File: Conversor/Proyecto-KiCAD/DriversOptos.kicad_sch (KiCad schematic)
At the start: 22 parts, among them U5 2ED21834-S06J, U6 2ED21834-S06J

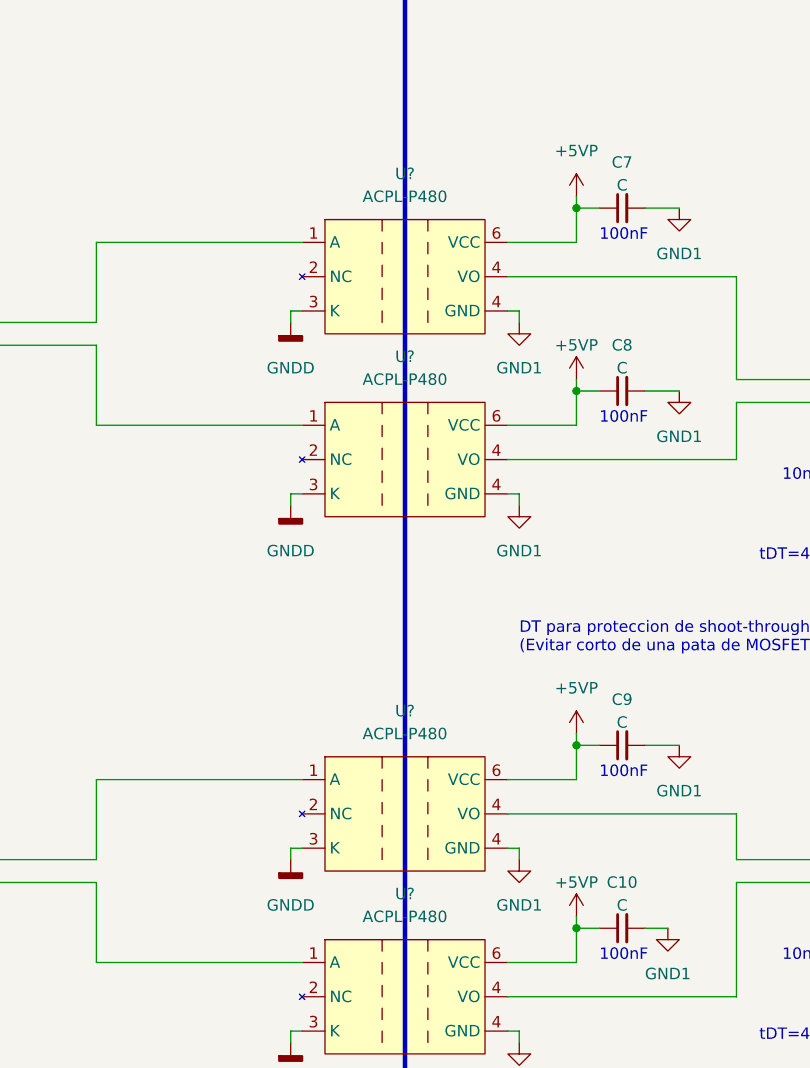
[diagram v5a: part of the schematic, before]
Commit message: Arreglar todos los errores del ERC
- Agregar flags de 'Not Connected' a pines flotantes
- Agregar resistencias 'falsas' para eliminar los errores de 'Power
input pin not connected to Power output pin'
- Agregar un GND1 conectado a PWR_FLAG para arreglar errores
- Además, agregar bien al proyecto la placa adaptadora importada a KiCad
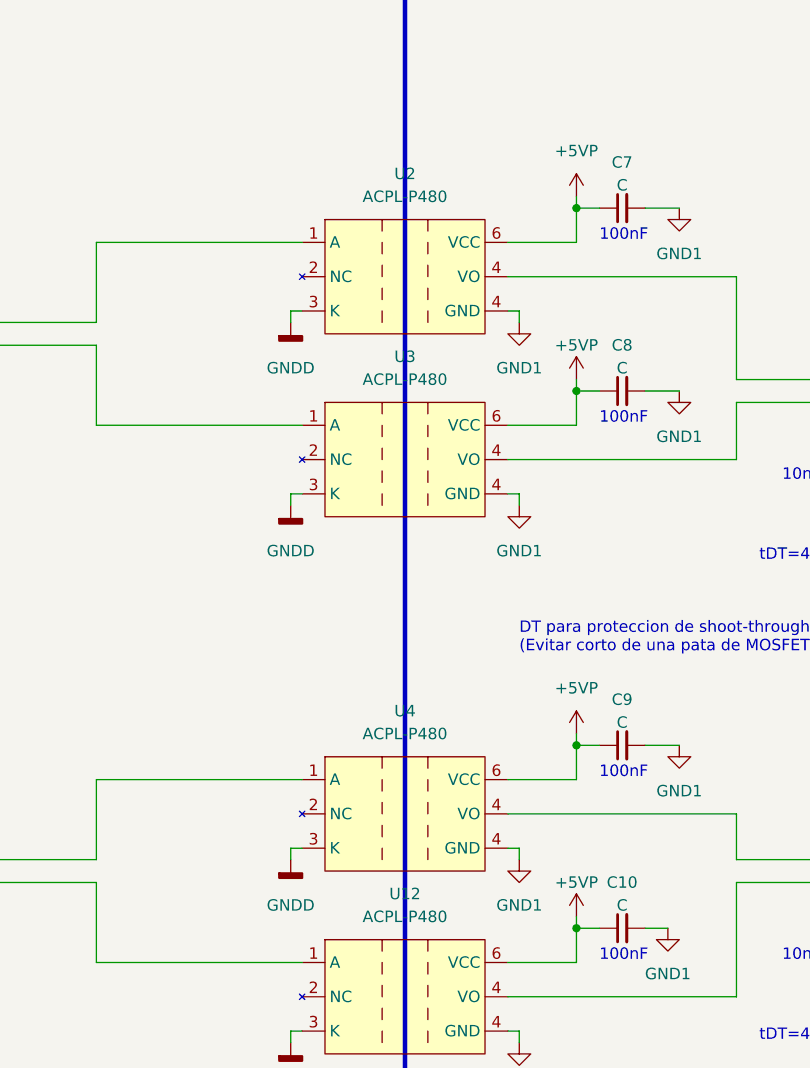
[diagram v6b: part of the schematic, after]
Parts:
- gave numbers to parts that had none: 4
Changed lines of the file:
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@@
   (symbol (lib_id "Componentes proyecto:ACPL-P480") (at 125.73 54.61 0) (unit 1)
     (in_bom yes) (on_board yes) (fields_autoplaced)
-    (property "Reference" "U?" (id 0) (at 125.73 43.18 0))
+    (property "Reference" "U2" (id 0) (at 125.73 43.18 0))
     (property "Value" "ACPL-P480" (id 1) (at 125.73 45.72 0))
     (property "Footprint" "" (id 2) (at 125.73 54.61 0)
@@
   (symbol (lib_id "Componentes proyecto:ACPL-P480") (at 125.73 134.62 0) (unit 1)
     (in_bom yes) (on_board yes) (fields_autoplaced)
-    (property "Reference" "U?" (id 0) (at 125.73 123.19 0))
+    (property "Reference" "U12" (id 0) (at 125.73 123.19 0))
     (property "Value" "ACPL-P480" (id 1) (at 125.73 125.73 0))
     (property "Footprint" "" (id 2) (at 125.73 134.62 0)
@@
   (symbol (lib_id "Componentes proyecto:ACPL-P480") (at 125.73 74.93 0) (unit 1)
     (in_bom yes) (on_board yes) (fields_autoplaced)
-    (property "Reference" "U?" (id 0) (at 125.73 63.5 0))
+    (property "Reference" "U3" (id 0) (at 125.73 63.5 0))
     (property "Value" "ACPL-P480" (id 1) (at 125.73 66.04 0))
     (property "Footprint" "" (id 2) (at 125.73 74.93 0)
@@
   (symbol (lib_id "Componentes proyecto:ACPL-P480") (at 125.73 114.3 0) (unit 1)
     (in_bom yes) (on_board yes) (fields_autoplaced)
-    (property "Reference" "U?" (id 0) (at 125.73 102.87 0))
+    (property "Reference" "U4" (id 0) (at 125.73 102.87 0))
     (property "Value" "ACPL-P480" (id 1) (at 125.73 105.41 0))
     (property "Footprint" "" (id 2) (at 125.73 114.3 0)

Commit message: Comenzar a asignar footprints a todos los componentes
- Agregado un header para conectar el módulo de tarjeta SD de Arduino
por SPI
- Los GNDs conectados por resistencias nulas son para conectar los GNDs
en caso de que fuera necesario
- Agregar una nota de aplicaión de aislación para I2C (creo que como
estan conectados SDAO y SDAI está bien)
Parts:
- C10, C11, C12, C13, C14, C15, C16, C7, C8, C9: footprint (none) -> Capacitor_SMD:C_1206_3216Metric_Pad1.33x1.80mm_HandSolder
- R1, R2, R3, R4, R5, R6: footprint (none) -> Resistor_SMD:R_1206_3216Metric_Pad1.30x1.75mm_HandSolder
- U12, U2, U3, U4: footprint (none) -> Package_SO:SSO-6_6.8x4.6mm_P1.27mm_Clearance7mm
- U5: footprint (none) -> Package_SO:SO-14_3.9x8.65mm_P1.27mm
- U6: footprint Package_SO:SOIC-14_3.9x8.7mm_P1.27mm -> Package_SO:SO-14_3.9x8.65mm_P1.27mm
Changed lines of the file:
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@@
       (effects (font (size 1.27 1.27)) (justify left))
     )
-    (property "Footprint" "" (id 2) (at 173.99 132.08 0)
+    (property "Footprint" "Capacitor_SMD:C_1206_3216Metric_Pad1.33x1.80mm_HandSolder" (id 2) (at 173.99 132.08 0)
       (effects (font (size 1.27 1.27)) hide)
     )
@@
     (property "Reference" "C9" (id 0) (at 149.86 101.6 90))
     (property "Value" "C" (id 1) (at 149.86 104.14 90))
-    (property "Footprint" "" (id 2) (at 149.86 106.68 0)
+    (property "Footprint" "Capacitor_SMD:C_1206_3216Metric_Pad1.33x1.80mm_HandSolder" (id 2) (at 149.86 106.68 0)
       (effects (font (size 1.27 1.27)) hide)
     )
@@
     (property "Reference" "U2" (id 0) (at 125.73 43.18 0))
     (property "Value" "ACPL-P480" (id 1) (at 125.73 45.72 0))
-    (property "Footprint" "" (id 2) (at 125.73 54.61 0)
+    (property "Footprint" "Package_SO:SSO-6_6.8x4.6mm_P1.27mm_Clearance7mm" (id 2) (at 125.73 54.61 0)
       (effects (font (size 1.27 1.27)) hide)
     )
@@
       (effects (font (size 1.27 1.27)) (justify left))
     )
-    (property "Footprint" "" (id 2) (at 204.47 120.65 0)
+    (property "Footprint" "Capacitor_SMD:C_1206_3216Metric_Pad1.33x1.80mm_HandSolder" (id 2) (at 204.47 120.65 0)
       (effects (font (size 1.27 1.27)) hide)
     )
@@
     (property "Reference" "C8" (id 0) (at 149.86 62.23 90))
     (property "Value" "C" (id 1) (at 149.86 64.77 90))
-    (property "Footprint" "" (id 2) (at 149.86 67.31 0)
+    (property "Footprint" "Capacitor_SMD:C_1206_3216Metric_Pad1.33x1.80mm_HandSolder" (id 2) (at 149.86 67.31 0)
       (effects (font (size 1.27 1.27)) hide)
     )
@@
     (property "Reference" "U12" (id 0) (at 125.73 123.19 0))
     (property "Value" "ACPL-P480" (id 1) (at 125.73 125.73 0))
-    (property "Footprint" "" (id 2) (at 125.73 134.62 0)
+    (property "Footprint" "Package_SO:SSO-6_6.8x4.6mm_P1.27mm_Clearance7mm" (id 2) (at 125.73 134.62 0)
       (effects (font (size 1.27 1.27)) hide)
     )
@@
     (property "Reference" "R3" (id 0) (at 212.09 111.76 90))
     (property "Value" "RonH" (id 1) (at 212.09 114.3 90))
-    (property "Footprint" "" (id 2) (at 212.344 115.824 90)
+    (property "Footprint" "Resistor_SMD:R_1206_3216Metric_Pad1.30x1.75mm_HandSolder" (id 2) (at 212.344 115.824 90)
       (effects (font (size 1.27 1.27)) hide)
     )
@@
       (effects (font (size 1.27 1.27)) (justify left))
     )
-    (property "Footprint" "Package_SO:SOIC-14_3.9x8.7mm_P1.27mm" (id 2) (at 191.77 121.92 0)
+    (property "Footprint" "Package_SO:SO-14_3.9x8.65mm_P1.27mm" (id 2) (at 191.77 121.92 0)
       (effects (font (size 1.27 1.27)) hide)
     )
@@
     (property "Reference" "U3" (id 0) (at 125.73 63.5 0))
     (property "Value" "ACPL-P480" (id 1) (at 125.73 66.04 0))
-    (property "Footprint" "" (id 2) (at 125.73 74.93 0)
+    (property "Footprint" "Package_SO:SSO-6_6.8x4.6mm_P1.27mm_Clearance7mm" (id 2) (at 125.73 74.93 0)
       (effects (font (size 1.27 1.27)) hide)
     )
@@
     (property "Reference" "C7" (id 0) (at 149.86 41.91 90))
     (property "Value" "C" (id 1) (at 149.86 44.45 90))
-    (property "Footprint" "" (id 2) (at 149.86 46.99 0)
+    (property "Footprint" "Capacitor_SMD:C_1206_3216Metric_Pad1.33x1.80mm_HandSolder" (id 2) (at 149.86 46.99 0)
       (effects (font (size 1.27 1.27)) hide)
     )
@@
     (property "Reference" "R5" (id 0) (at 218.44 68.58 90))
     (property "Value" "RS" (id 1) (at 218.44 73.66 90))
-    (property "Footprint" "" (id 2) (at 218.694 70.104 90)
+    (property "Footprint" "Resistor_SMD:R_1206_3216Metric_Pad1.30x1.75mm_HandSolder" (id 2) (at 218.694 70.104 90)
       (effects (font (size 1.27 1.27)) hide)
     )
@@
     (property "Reference" "C13" (id 0) (at 184.1563 45.72 90))
     (property "Value" "CVCC" (id 1) (at 184.1563 48.26 90))
-    (property "Footprint" "" (id 2) (at 184.15 52.07 0)
+    (property "Footprint" "Capacitor_SMD:C_1206_3216Metric_Pad1.33x1.80mm_HandSolder" (id 2) (at 184.15 52.07 0)
       (effects (font (size 1.27 1.27)) hide)
     )
@@
     (property "Reference" "R2" (id 0) (at 212.09 78.74 90))
     (property "Value" "RonL" (id 1) (at 212.09 81.28 90))
-    (property "Footprint" "" (id 2) (at 212.344 75.184 90)
+    (property "Footprint" "Resistor_SMD:R_1206_3216Metric_Pad1.30x1.75mm_HandSolder" (id 2) (at 212.344 75.184 90)
       (effects (font (size 1.27 1.27)) hide)
     )
@@
     (property "Reference" "R1" (id 0) (at 212.09 58.42 90))
     (property "Value" "RonH" (id 1) (at 212.09 60.96 90))
-    (property "Footprint" "" (id 2) (at 212.344 62.484 90)
+    (property "Footprint" "Resistor_SMD:R_1206_3216Metric_Pad1.30x1.75mm_HandSolder" (id 2) (at 212.344 62.484 90)
       (effects (font (size 1.27 1.27)) hide)
     )
@@
     (property "Reference" "C10" (id 0) (at 149.86 121.92 90))
     (property "Value" "C" (id 1) (at 149.86 124.46 90))
-    (property "Footprint" "" (id 2) (at 149.86 127 0)
+    (property "Footprint" "Capacitor_SMD:C_1206_3216Metric_Pad1.33x1.80mm_HandSolder" (id 2) (at 149.86 127 0)
       (effects (font (size 1.27 1.27)) hide)
     )
@@
       (effects (font (size 1.27 1.27)) (justify left))
     )
-    (property "Footprint" "" (id 2) (at 173.99 78.74 0)
+    (property "Footprint" "Capacitor_SMD:C_1206_3216Metric_Pad1.33x1.80mm_HandSolder" (id 2) (at 173.99 78.74 0)
       (effects (font (size 1.27 1.27)) hide)
     )
@@
       (effects (font (size 1.27 1.27)) (justify left))
     )
-    (property "Footprint" "" (id 2) (at 204.47 67.31 0)
+    (property "Footprint" "Capacitor_SMD:C_1206_3216Metric_Pad1.33x1.80mm_HandSolder" (id 2) (at 204.47 67.31 0)
       (effects (font (size 1.27 1.27)) hide)
     )
@@
     (property "Reference" "R6" (id 0) (at 218.44 121.92 90))
     (property "Value" "RS" (id 1) (at 218.44 127 90))
-    (property "Footprint" "" (id 2) (at 218.694 123.444 90)
+    (property "Footprint" "Resistor_SMD:R_1206_3216Metric_Pad1.30x1.75mm_HandSolder" (id 2) (at 218.694 123.444 90)
       (effects (font (size 1.27 1.27)) hide)
     )
@@
     (property "Reference" "C14" (id 0) (at 184.1563 99.06 90))
     (property "Value" "CVCC" (id 1) (at 184.1563 101.6 90))
-    (property "Footprint" "" (id 2) (at 184.15 105.41 0)
+    (property "Footprint" "Capacitor_SMD:C_1206_3216Metric_Pad1.33x1.80mm_HandSolder" (id 2) (at 184.15 105.41 0)
       (effects (font (size 1.27 1.27)) hide)
     )
@@
     (property "Reference" "R4" (id 0) (at 212.09 132.08 90))
     (property "Value" "RonL" (id 1) (at 212.09 134.62 90))
-    (property "Footprint" "" (id 2) (at 212.344 128.524 90)
+    (property "Footprint" "Resistor_SMD:R_1206_3216Metric_Pad1.30x1.75mm_HandSolder" (id 2) (at 212.344 128.524 90)
       (effects (font (size 1.27 1.27)) hide)
     )
@@
       (effects (font (size 1.27 1.27)) (justify left))
     )
-    (property "Footprint" "" (id 2) (at 191.77 68.58 0)
+    (property "Footprint" "Package_SO:SO-14_3.9x8.65mm_P1.27mm" (id 2) (at 191.77 68.58 0)
       (effects (font (size 1.27 1.27)) hide)
     )
@@
     (property "Reference" "U4" (id 0) (at 125.73 102.87 0))
     (property "Value" "ACPL-P480" (id 1) (at 125.73 105.41 0))
-    (property "Footprint" "" (id 2) (at 125.73 114.3 0)
-      (effects (font (size 1.27 1.27)) hide)
-    )
+    (property "Footprint" "Package_SO:SSO-6_6.8x4.6mm_P1.27mm_Clearance7mm" (id 2) (at 125.73 114.3 0)
+      (effects (font (size 1.27 1.27)) hide)
+    )
